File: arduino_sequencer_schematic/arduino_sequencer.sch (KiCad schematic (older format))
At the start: 160 parts, among them J1 AudioJack, J10 AudioJack, J11 AudioJack, J12 AudioJack, J13 AudioJack, J14 AudioJack, J15 AudioJack, J16 Conn_02x05, J2 AudioJack, J3 AudioJack, J4 AudioJack, J5 AudioJack, J6 AudioJack, J7 AudioJack, J8 AudioJack, J9 AudioJack, Q1 2N3904, Q10 2N3904, Q11 2N3904, Q2 2N3904, Q3 2N3904, Q4 2N3904, Q5 2N3904, Q6 2N3904, Q7 2N3904, Q8 2N3904, Q9 2N3904, SW1 SW_Push, SW2 SW_SPST, SW3 SW_Push, SW4 SW_Push, SW5 SW_SPST, SW6 SW_SPST, U1 74HC595, U2 TL084, U3 TL084, U4 L7805

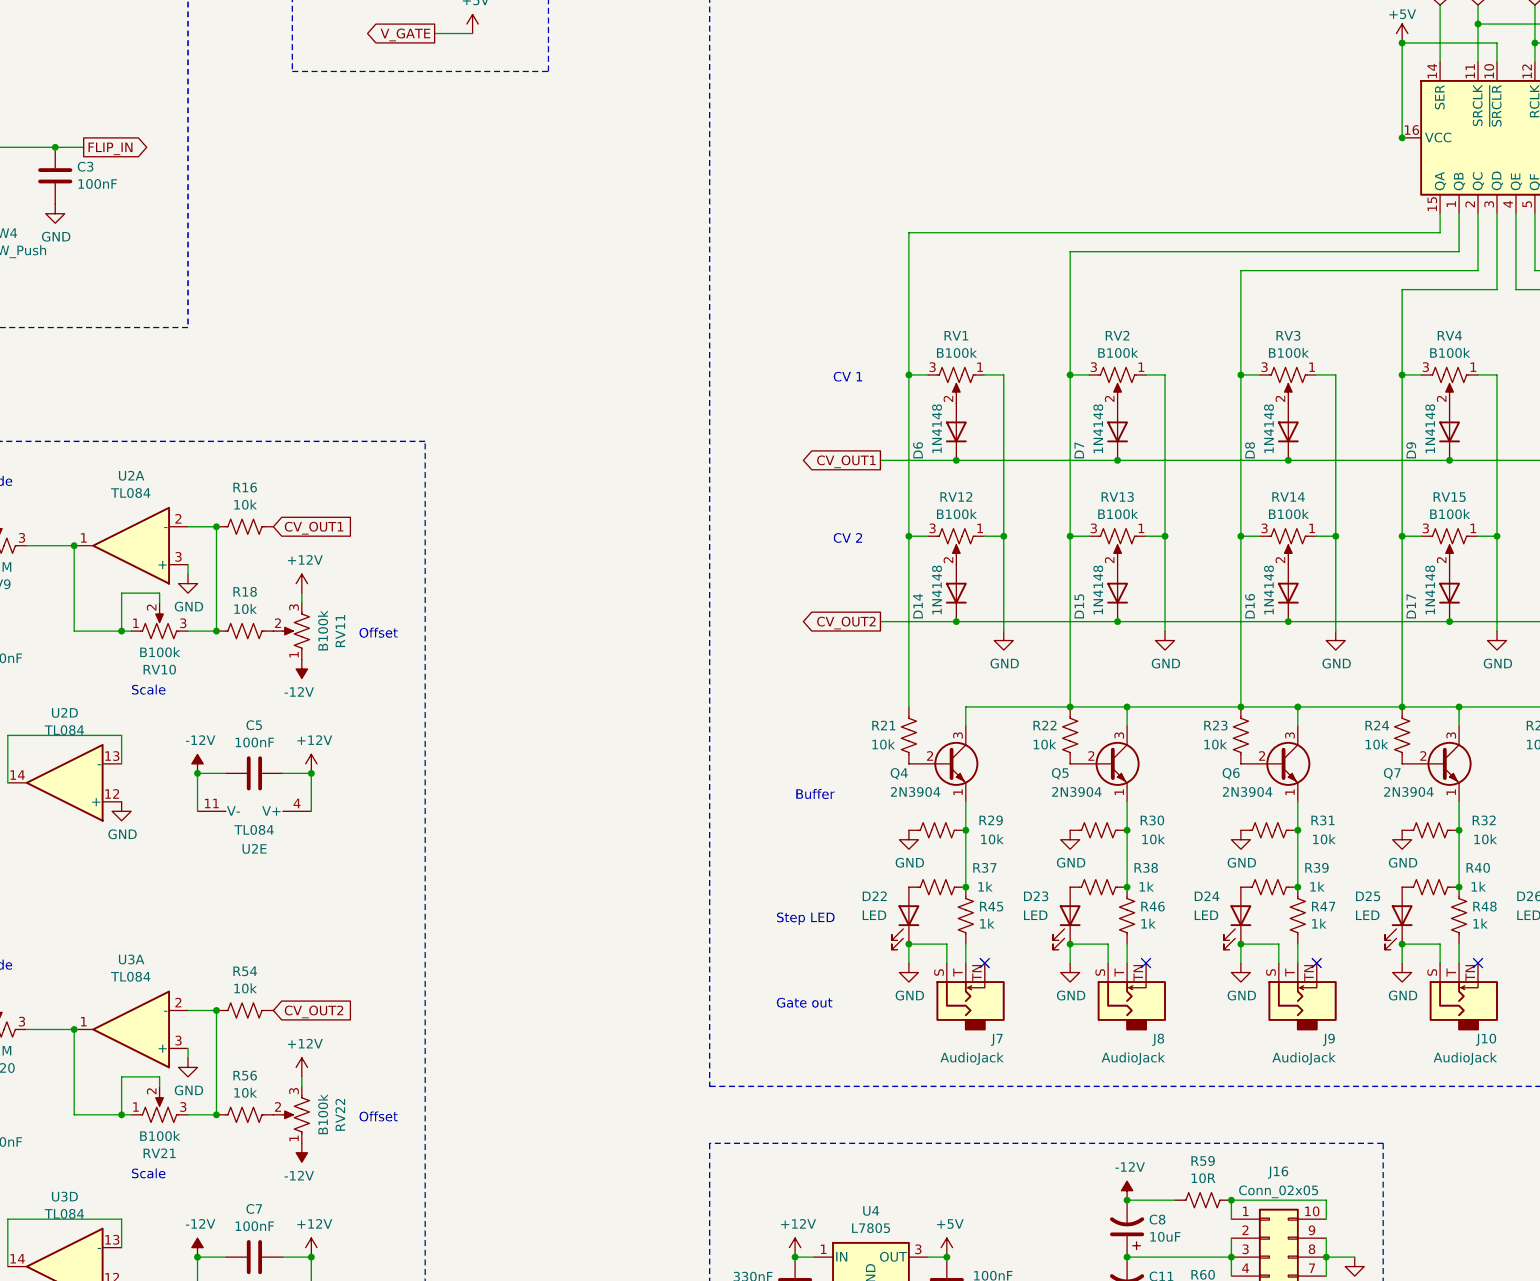
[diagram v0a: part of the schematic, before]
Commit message: Chaged scale pot values to 50k
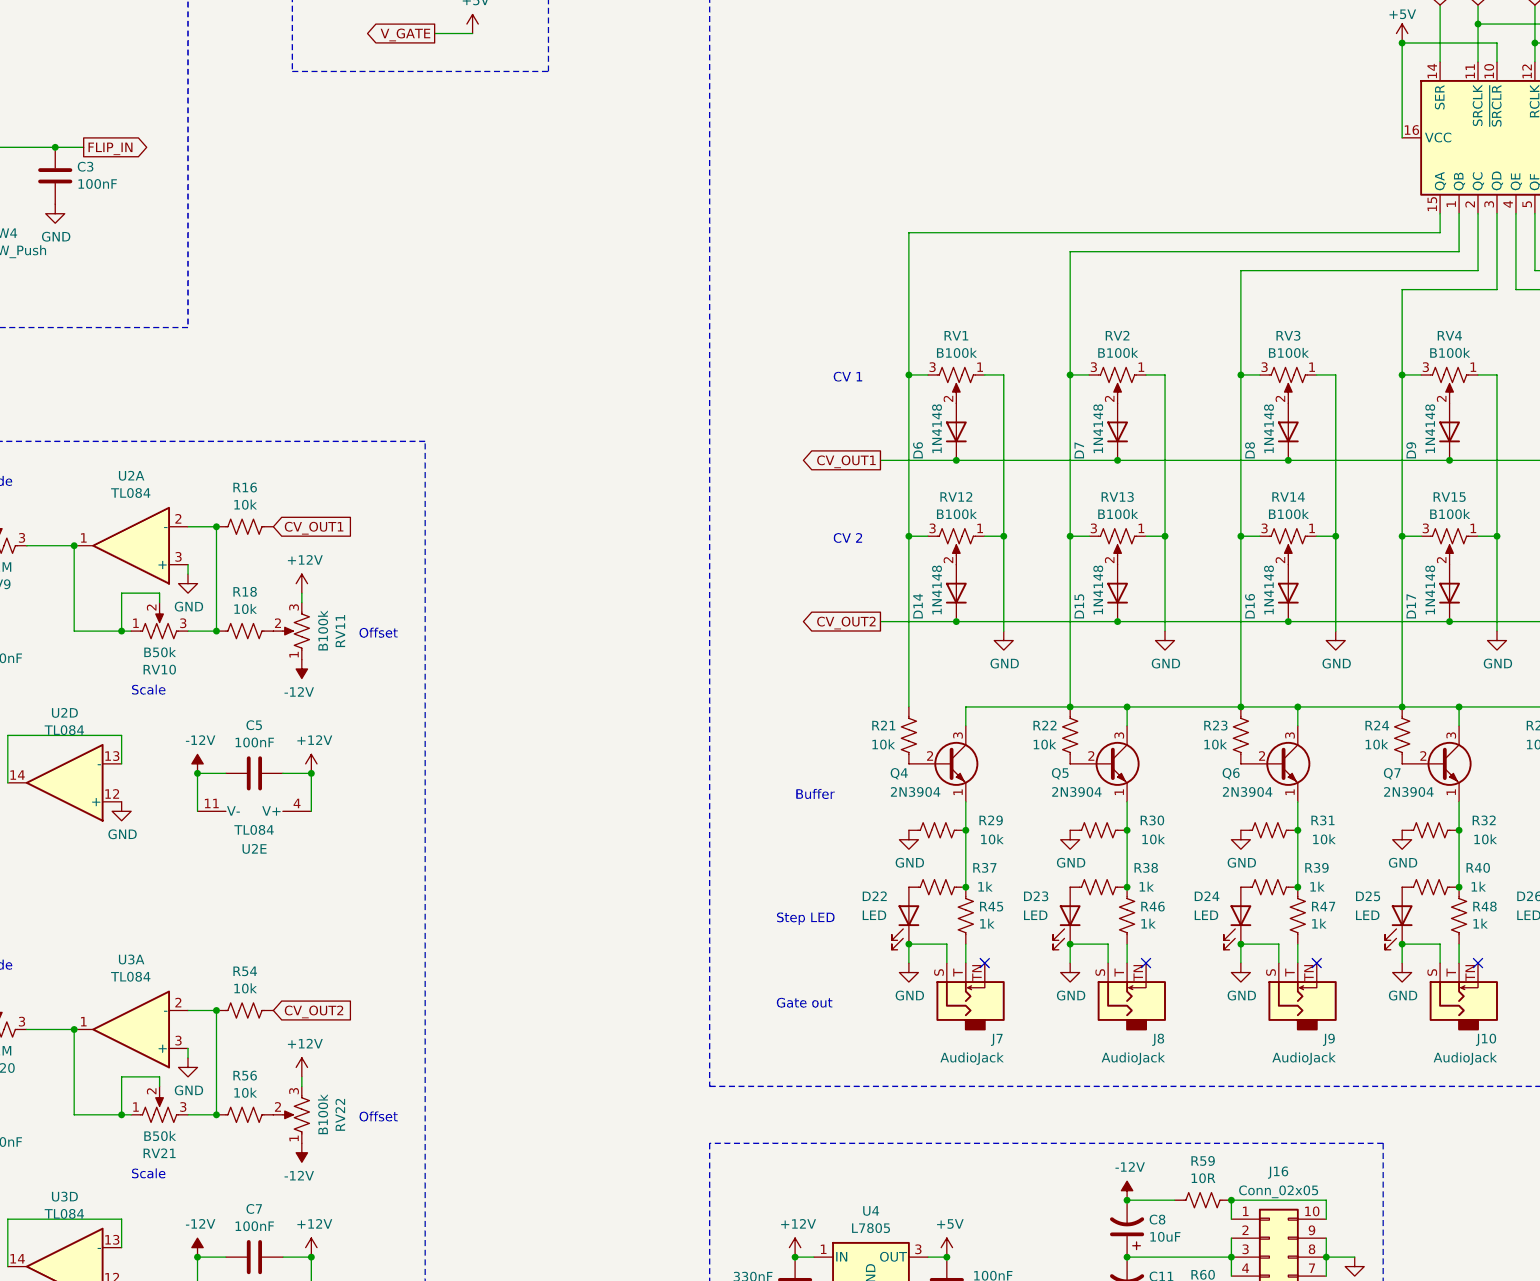
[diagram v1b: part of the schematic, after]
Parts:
- RV10, RV21: value B100k -> B50k
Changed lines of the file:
@@
 Text GLabel 8500 2000 3    50   Output ~ 0
 DEC_LED
-Connection ~ 10750 4150
 $Comp
 L Connector_Generic:Conn_02x05_Counter_Clockwise J16
@@
 P 4200 9300
 F 0 "RV21" V 3995 9300 50  0000 C CNN
-F 1 "B100k" V 4086 9300 50  0000 C CNN
+F 1 "B50k" V 4086 9300 50  0000 C CNN
 F 2 "" H 4200 9300 50  0001 C CNN
 F 3 "~" H 4200 9300 50  0001 C CNN
@@
 P 4200 6750
 F 0 "RV10" V 3995 6750 50  0000 C CNN
-F 1 "B100k" V 4086 6750 50  0000 C CNN
+F 1 "B50k" V 4086 6750 50  0000 C CNN
 F 2 "" H 4200 6750 50  0001 C CNN
 F 3 "~" H 4200 6750 50  0001 C CNN

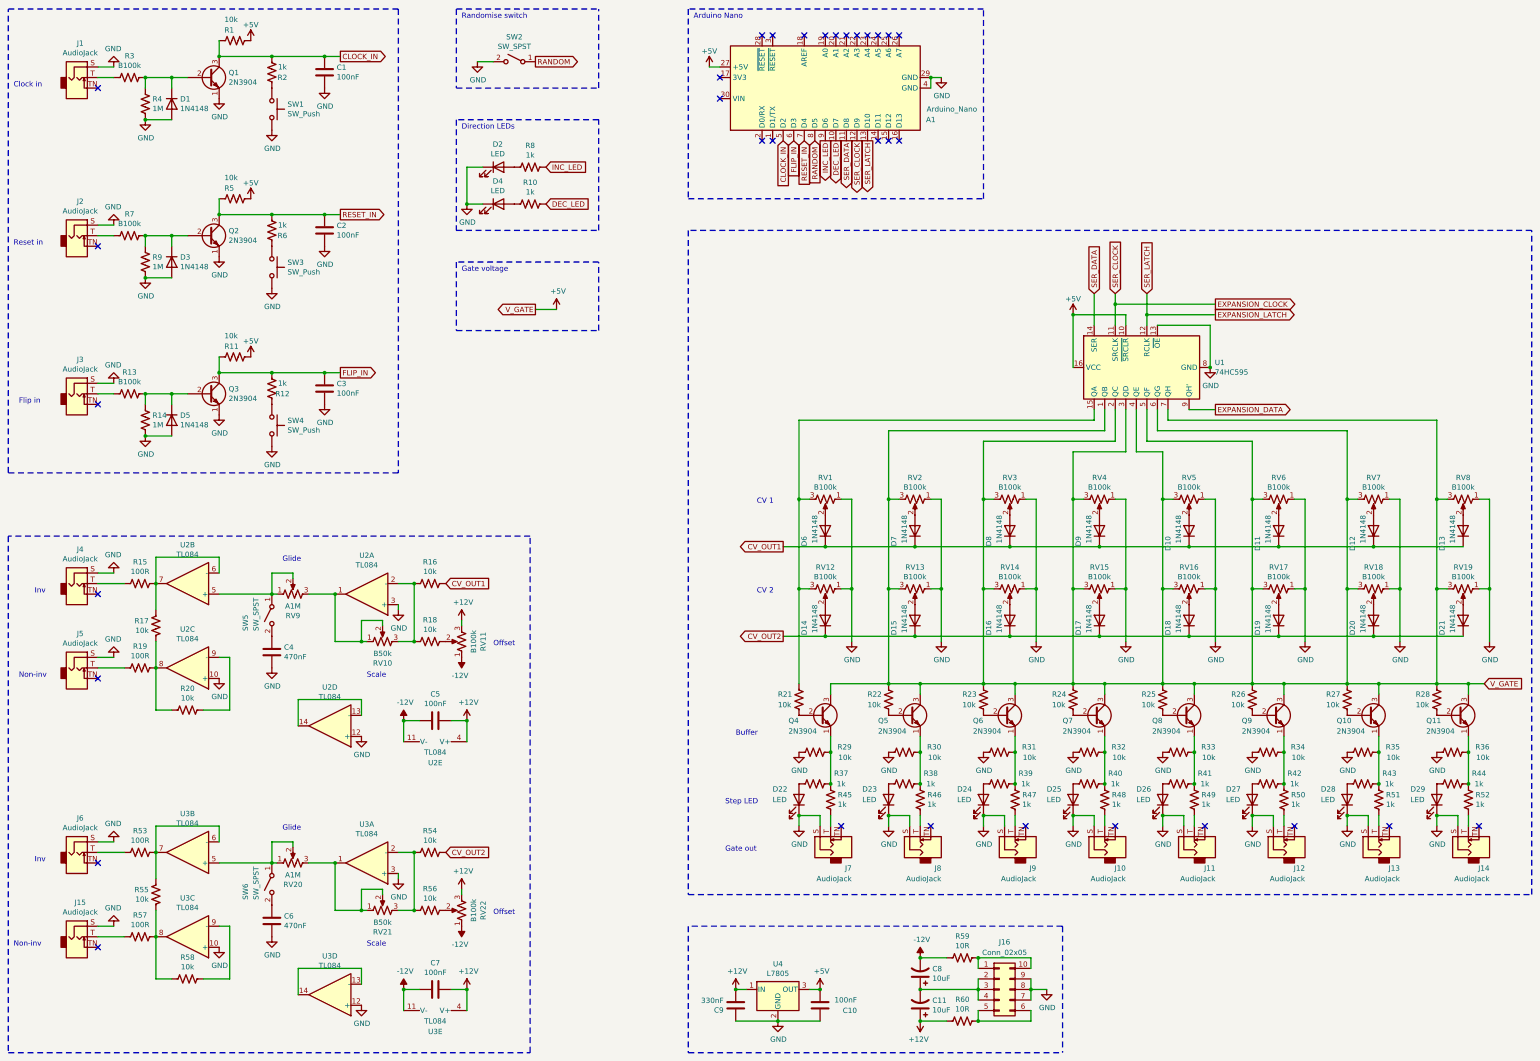
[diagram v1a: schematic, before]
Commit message: Fixed errors in CV interver and gate buffers
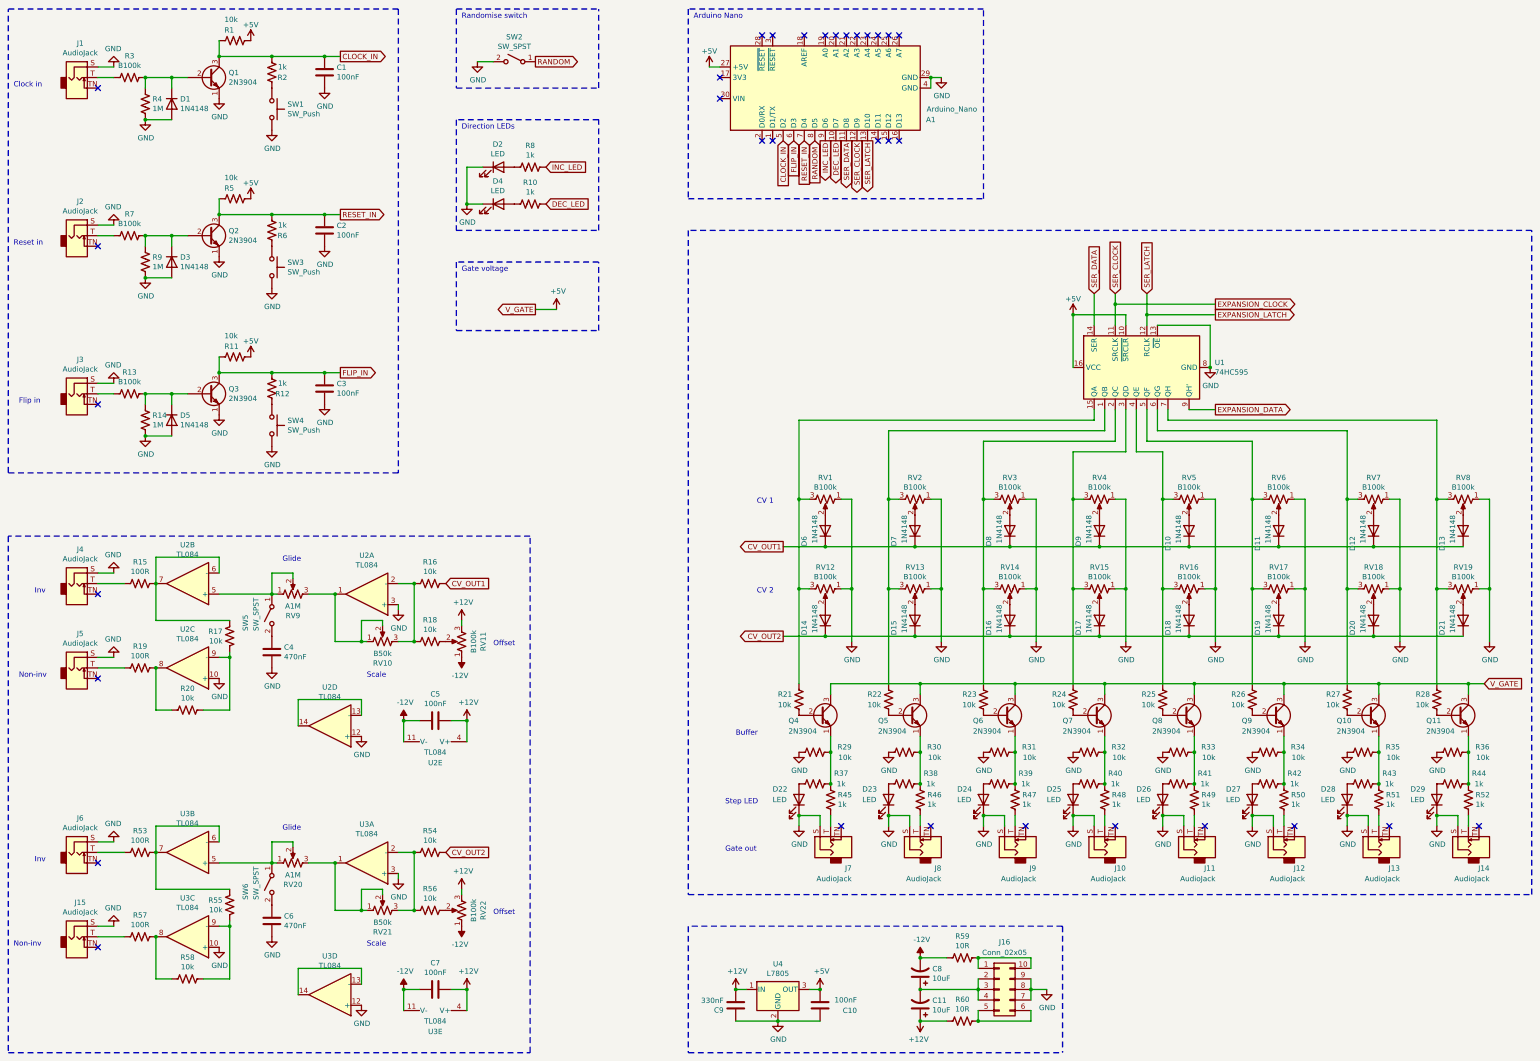
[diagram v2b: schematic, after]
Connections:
- net +5V: no longer R22.1, R23.1, R24.1, R25.1, R26.1, R27.1, R28.1, RV13.3, RV14.3, RV15.3, RV16.3, RV17.3, RV18.3, RV19.3, RV2.3, RV3.3, RV4.3, RV5.3, RV6.3, RV7.3, RV8.3, U1.1 (QB), U1.2 (QC), U1.3 (QD), U1.4 (QE), U1.5 (QF), U1.6 (QG), U1.7 (QH)
- net at R57.1, R58.2, U3.8: no longer R55.1
- net at R58.1, U3.9 (-): now also R55.1
- net at R19.1, R20.2, U2.8: no longer R17.1
- net at R20.1, U2.9 (-): now also R17.1
- new net: R22.1, RV13.3, RV2.3, U1.1 (QB)
- new net: R23.1, RV14.3, RV3.3, U1.2 (QC)
- new net: R24.1, RV15.3, RV4.3, U1.3 (QD)
- new net: R25.1, RV16.3, RV5.3, U1.4 (QE)
- new net: R26.1, RV17.3, RV6.3, U1.5 (QF)
- new net: R27.1, RV18.3, RV7.3, U1.6 (QG)
- new net: R28.1, RV19.3, RV8.3, U1.7 (QH)
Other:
- moved on the sheet: R17, R55
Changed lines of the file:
@@
 Text GLabel 14650 7150 2    50   Input ~ 0
 V_GATE
-Wire Wire Line
-	8450 7150 9000 7150
-Wire Wire Line
-	9300 7150 9900 7150
-Wire Wire Line
-	10200 7150 10750 7150
-Wire Wire Line
-	11050 7150 11600 7150
 $Comp
 L Device:R_US R26
@@
 	1    0    0    -1
 $EndComp
-Wire Wire Line
-	11900 7150 12450 7150
-Wire Wire Line
-	12750 7150 13350 7150
-Wire Wire Line
-	13650 7150 14200 7150
 Wire Wire Line
 	14650 7150 14500 7150
@@
 L Device:R_US R55
 U 1 1 60C29BC0
-P 2050 9150
-F 0 "R55" H 1982 9104 50  0000 R CNN
-F 1 "10k" H 1982 9195 50  0000 R CNN
-F 2 "" V 2090 9140 50  0001 C CNN
-F 3 "~" H 2050 9150 50  0001 C CNN
-	1    2050 9150
+P 2750 9250
+F 0 "R55" H 2682 9204 50  0000 R CNN
+F 1 "10k" H 2682 9295 50  0000 R CNN
+F 2 "" V 2790 9240 50  0001 C CNN
+F 3 "~" H 2750 9250 50  0001 C CNN
+	1    2750 9250
 	1    0    0    1
 $EndComp
@@
 	5000 10050 4850 10050
 Connection ~ 5000 10050
-Connection ~ 9000 7150
-Wire Wire Line
-	9000 7150 9300 7150
-Connection ~ 9900 7150
-Wire Wire Line
-	9900 7150 10200 7150
-Connection ~ 10750 7150
-Wire Wire Line
-	10750 7150 11050 7150
-Connection ~ 11600 7150
-Wire Wire Line
-	11600 7150 11900 7150
-Connection ~ 12450 7150
-Wire Wire Line
-	12450 7150 12750 7150
-Connection ~ 13350 7150
-Wire Wire Line
-	13350 7150 13650 7150
-Connection ~ 14200 7150
-Wire Wire Line
-	14200 7150 14500 7150
 Wire Wire Line
 	3750 8850 3750 9300
@@
 L Device:R_US R17
 U 1 1 6126E4BA
-P 2050 6600
-F 0 "R17" H 1982 6554 50  0000 R CNN
-F 1 "10k" H 1982 6645 50  0000 R CNN
-F 2 "" V 2090 6590 50  0001 C CNN
-F 3 "~" H 2050 6600 50  0001 C CNN
-	1    2050 6600
+P 2750 6700
+F 0 "R17" H 2682 6654 50  0000 R CNN
+F 1 "10k" H 2682 6745 50  0000 R CNN
+F 2 "" V 2790 6690 50  0001 C CNN
+F 3 "~" H 2750 6700 50  0001 C CNN
+	1    2750 6700
 	1    0    0    1
 $EndComp
@@
 	6250 3150 4900 3150
 Wire Wire Line
-	2050 6750 2050 7000
-Wire Wire Line
-	2050 6200 2050 6450
-Wire Wire Line
-	2050 9300 2050 9550
-Wire Wire Line
-	2050 8750 2050 9000
-Wire Wire Line
 	1650 6100 1500 6100
 Wire Wire Line
@@
 	1500 8650 1650 8650
 Connection ~ 10750 3650
+Wire Wire Line
+	8450 7150 9300 7150
+Wire Wire Line
+	9300 7150 10200 7150
+Wire Wire Line
+	10200 7150 11050 7150
+Wire Wire Line
+	11050 7150 11900 7150
+Wire Wire Line
+	11900 7150 12750 7150
+Wire Wire Line
+	12750 7150 13650 7150
+Wire Wire Line
+	13650 7150 14500 7150
+Wire Wire Line
+	2750 9400 2750 9450
+Connection ~ 2750 9450
+Wire Wire Line
+	2750 9100 2050 9100
+Wire Wire Line
+	2050 8750 2050 9100
+Wire Wire Line
+	2750 6900 2750 6850
+Connection ~ 2750 6900
+Wire Wire Line
+	2750 6550 2050 6550
+Wire Wire Line
+	2050 6200 2050 6550
 $EndSCHEMATC
